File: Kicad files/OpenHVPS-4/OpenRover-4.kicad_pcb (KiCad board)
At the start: 2 copper layers, 40.6 x 20.8 mm, 70 parts, among them J2 Conn_01x03_Male, Q1 FQT7N10, Q2 BC846A, Q3 MMDT3906, U1 MAX6008AEUR+T, U2 74HC14, U3 MAX4162, U4 CD14538BM

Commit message: Updated C22 to 369pF
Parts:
- C22: value 1nF -> 360pF

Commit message: Generated gerber files
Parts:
- moved H2 1.03 mm to (164.1, 74.6)
- moved R14 0.73 mm to (147.2, 65.0)
- moved H2 0.44 mm to (164.7, 70.5)
- moved REF** 0.39 mm to (164.6, 59.2)
- moved REF** 0.39 mm to (164.6, 62.0)
- moved R1 0.38 mm to (164.5, 66.4)
- moved D2 0.31 mm to (134.5, 59.8)
- moved R21 0.27 mm to (142.0, 74.9)
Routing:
- net Net-(H2-Pad1): track 6.62 -> 8.29 mm
- net +2V5: track 18.1 -> 17.5 mm

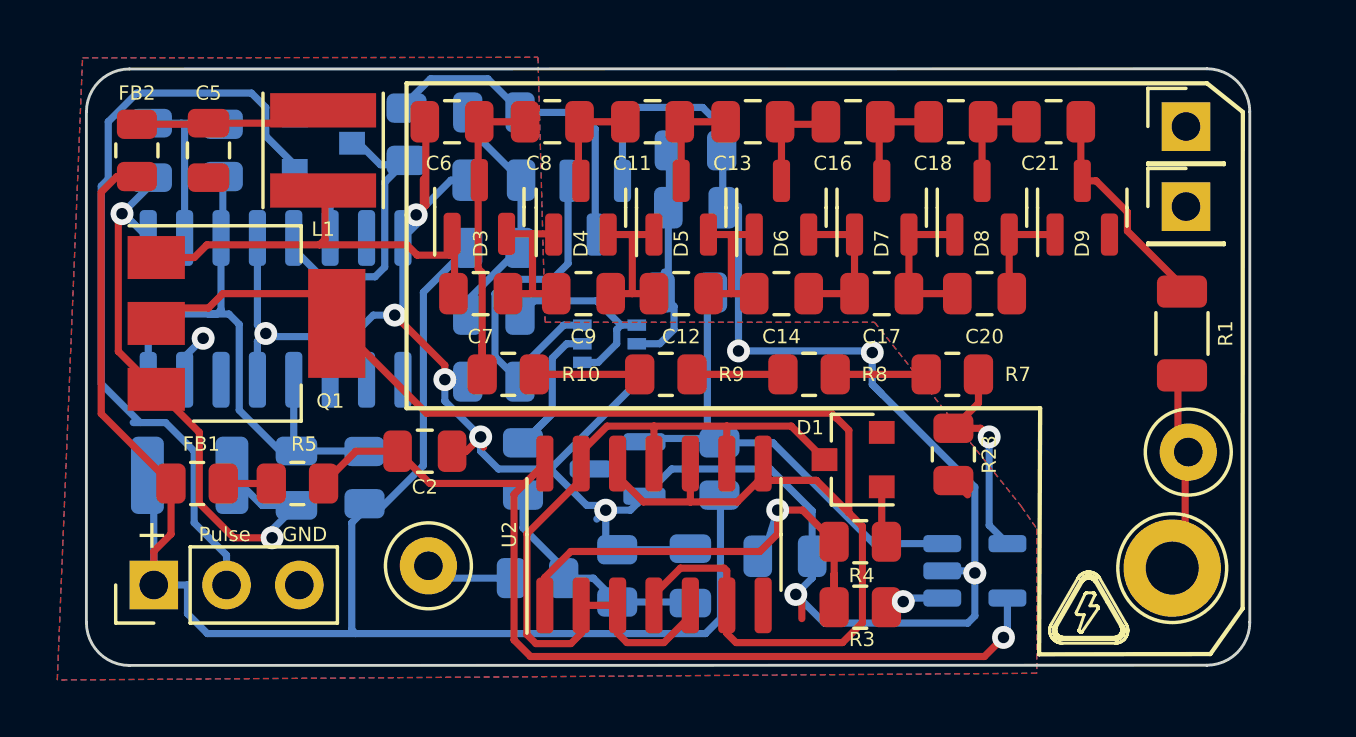
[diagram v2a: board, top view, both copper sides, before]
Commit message: Changed D1 D2 added F1 and updated BOM
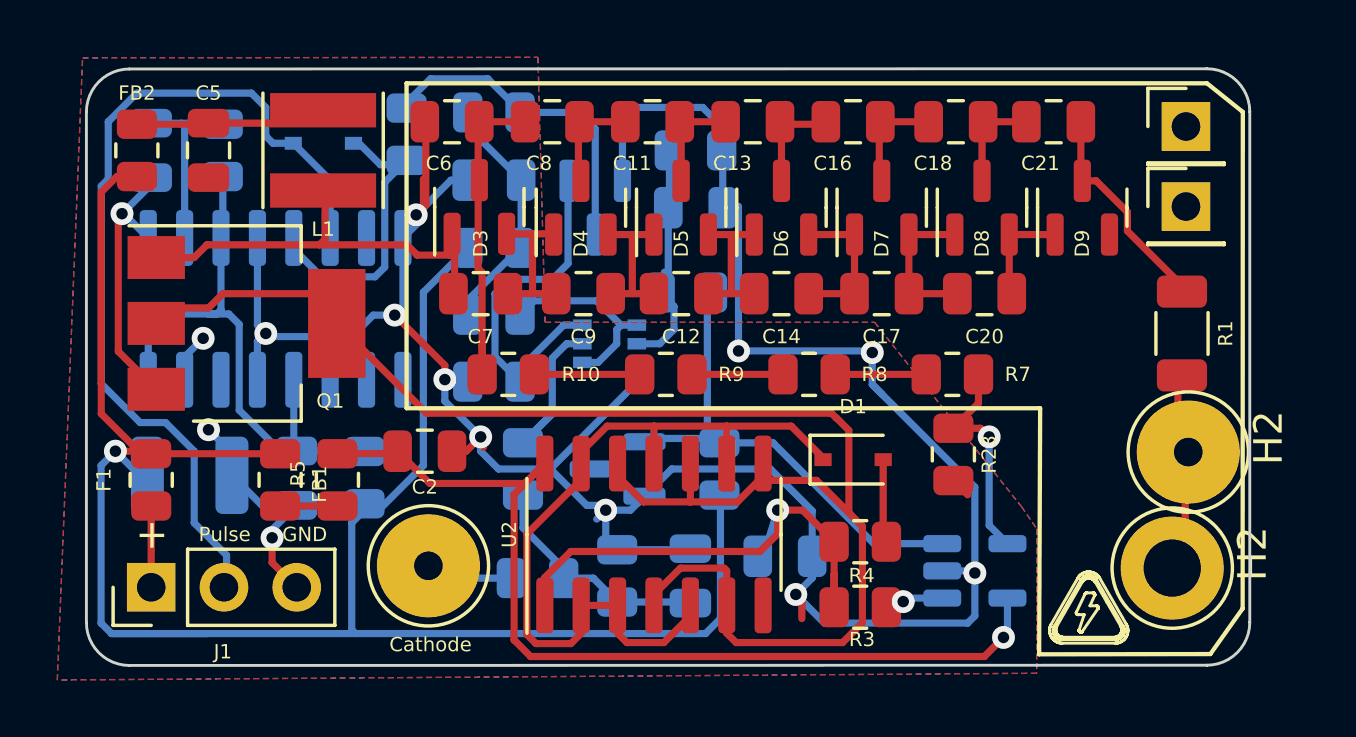
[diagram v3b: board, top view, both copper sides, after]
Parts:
- removed J2: Conn_01x03_Male, Connector_PinHeader_2.54mm:PinHeader_1x03_P2.54mm_Vertical
- added F1: Polyfuse, Resistor_SMD:R_0805_2012Metric, F.Cu at (128.5, 71.5)
- added J1: Conn_01x03_Male, Connector_PinHeader_2.54mm:PinHeader_1x03_P2.54mm_Vertical, F.Cu at (128.5, 75.2)
- D1, D2: value BAS16 -> BAS16J; footprint Diode_SMD:D_SOT-23_ANK -> Diode_SMD:D_SOD-323
- H1, H2: footprint TestPoint:TestPoint_Loop_D2.50mm_Drill1.0mm -> TestPoint:TestPoint_Loop_D3.80mm_Drill2.0mm
- H2: footprint TestPoint:TestPoint_Loop_D2.50mm_Drill1.85mm -> TestPoint:TestPoint_Loop_D3.80mm_Drill2.0mm
- moved FB1 2.90 mm to (133.0, 71.5), turned to -90 degrees
- moved R5 1.40 mm to (135.0, 71.5), turned to -90 degrees
- turned D1 to 0 degrees
- turned D2 to 180 degrees
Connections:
- net no_connect_(D9-Pad2) renamed Net-(D9-Pad2)
- net no_connect_(U1-Pad3) renamed Net-(U1-Pad3)
- net no_connect_(U4-Pad10) renamed Net-(U4-Pad10)
- net no_connect_(U4-Pad14) renamed Net-(U4-Pad14)
- net no_connect_(U4-Pad7) renamed Net-(U4-Pad7)
- net no_connect_(U4-Pad9) renamed Net-(U4-Pad9)
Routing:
- net +3V3: track 63.2 -> 72.2 mm, vias 0 -> 1
- net GND: track 122.0 -> 118.3 mm, vias 13 -> 14
- net Net-(F1-Pad1): track 0.00 -> 2.84 mm
- net Net-(D1-Pad2): track 1.75 -> 2.91 mm
- net Net-(C2-Pad1): track 34.6 -> 33.7 mm

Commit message: Fixed DRC erros in layout, changed final BOM
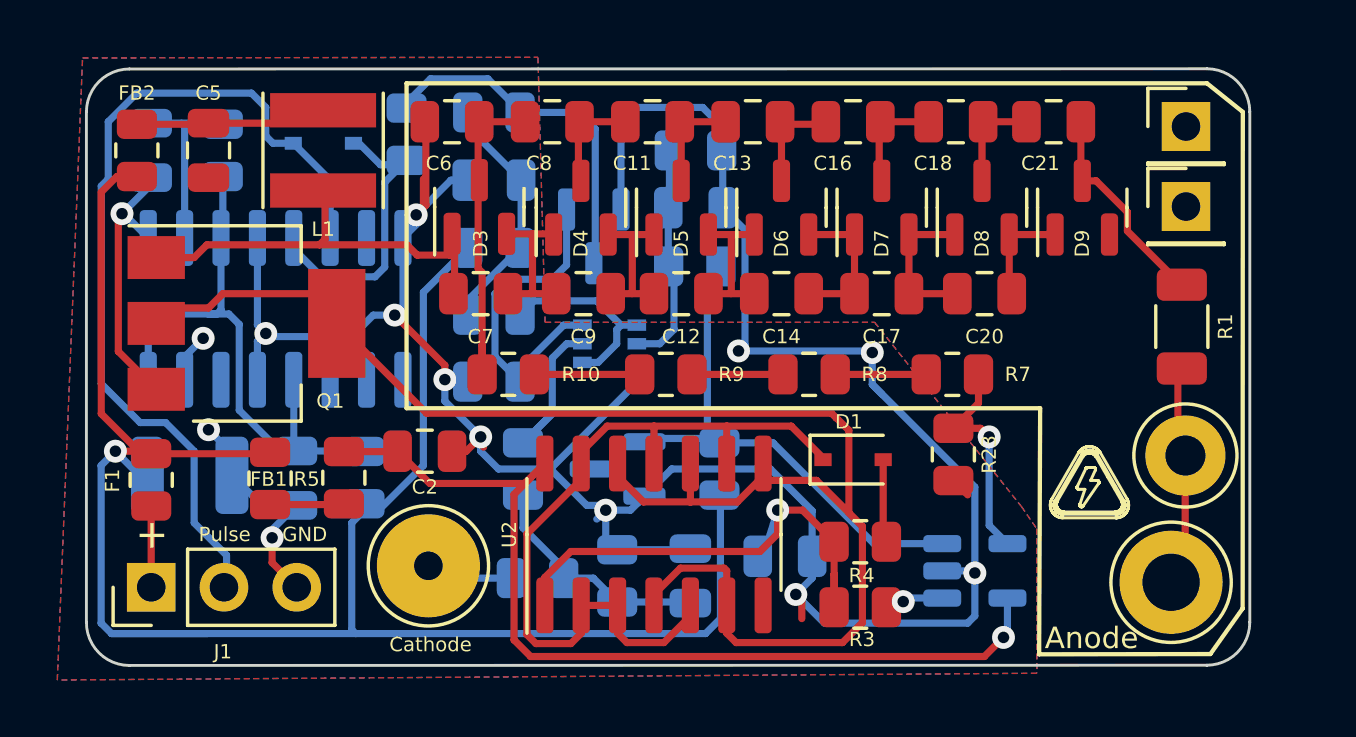
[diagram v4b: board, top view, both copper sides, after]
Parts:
- H2: footprint TestPoint:TestPoint_Loop_D3.80mm_Drill2.0mm -> TestPoint:TestPoint_Loop_D3.50mm_Drill1.4mm_Beaded
- moved Q2 1.00 mm to (143.9, 63.0)
- moved R14 0.96 mm to (147.5, 64.0)
- moved H2 0.50 mm to (164.1, 75.1)
- moved FB1 0.35 mm to (132.7, 71.5)
- moved R1 0.24 mm to (164.5, 66.2)
- moved R5 0.24 mm to (135.2, 71.4)
- moved H2 0.16 mm to (164.6, 70.7)
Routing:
- net GND: track 118.3 -> 119.7 mm
- net +2V5: track 17.5 -> 18.5 mm
- net Net-(Q2-Pad3): track 11.8 -> 12.8 mm
- net Net-(Q2-Pad1): track 13.4 -> 12.4 mm
- net Net-(FB1-Pad2): track 2.00 -> 2.59 mm
